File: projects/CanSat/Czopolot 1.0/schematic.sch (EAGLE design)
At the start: 6 parts

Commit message: File update
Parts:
- U$1: device PyBoard 1.1 footprint:PYBOARD1.1 -> SobieskiSat2:PYBOARD1.1
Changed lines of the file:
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@@
 </classes>
 <parts>
-<part name="U$1" library="PyBoard 1.1 footprint" deviceset="PYBOARD1.1" device=""/>
+<part name="U$1" library="SobieskiSat2" deviceset="PYBOARD1.1" device=""/>
 <part name="ULTIMATE_GPS" library="pinhead" library_urn="urn:adsk.eagle:library:325" deviceset="PINHD-1X4" device="" package3d_urn="urn:adsk.eagle:package:22407/2"/>
 <part name="U$2" library="SobieskiSat2" deviceset="SX1280" device="EXT" value="SX1280EXT"/>

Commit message: Work work..
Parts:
- U$2: value SX1280EXT -> SX1280; device SobieskiSat2:SX1280EXT -> SobieskiSat2:SX1280
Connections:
- new net BAT+: U$1.VBAT
- new net DIO1: U$1.X3, U$2.DIO1
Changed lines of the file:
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@@
 <part name="U$1" library="SobieskiSat2" deviceset="PYBOARD1.1" device=""/>
 <part name="ULTIMATE_GPS" library="pinhead" library_urn="urn:adsk.eagle:library:325" deviceset="PINHD-1X4" device="" package3d_urn="urn:adsk.eagle:package:22407/2"/>
-<part name="U$2" library="SobieskiSat2" deviceset="SX1280" device="EXT" value="SX1280EXT"/>
+<part name="U$2" library="SobieskiSat2" deviceset="SX1280" device="" value="SX1280"/>
 <part name="GND1" library="supply1" library_urn="urn:adsk.eagle:library:371" deviceset="GND" device=""/>
 <part name="X1" library="SobieskiSat2" deviceset="SMACONNECTOR" device="" package3d_urn="urn:adsk.eagle:package:6240946/1"/>
@@
 <part name="P+4" library="supply1" library_urn="urn:adsk.eagle:library:371" deviceset="VCC" device=""/>
 <part name="P+5" library="supply1" library_urn="urn:adsk.eagle:library:371" deviceset="VCC" device=""/>
+<part name="GND5" library="supply1" library_urn="urn:adsk.eagle:library:371" deviceset="GND" device=""/>
 </parts>
 <sheets>
@@
 <instance part="P+5" gate="VCC" x="-30.48" y="17.78" smashed="yes" rot="R90">
 <attribute name="VALUE" x="-27.94" y="15.24" size="1.778" layer="96" rot="R180"/>
+</instance>
+<instance part="GND5" gate="1" x="-50.8" y="7.62" smashed="yes" rot="R270">
+<attribute name="VALUE" x="-53.34" y="10.16" size="1.778" layer="96" rot="R270"/>
 </instance>
 </instances>
@@
 </segment>
 </net>
+<net name="BAT+" class="0">
+<segment>
+<pinref part="U$1" gate="G$1" pin="VBAT"/>
+<wire x1="-22.86" y1="7.62" x2="-25.4" y2="7.62" width="0.1524" layer="91"/>
+<label x="-25.4" y="7.62" size="1.778" layer="95" rot="R180" xref="yes"/>
+</segment>
+</net>
+<net name="BAT-" class="0">
+<segment>
+<pinref part="GND5" gate="1" pin="GND"/>
+<wire x1="-48.26" y1="7.62" x2="-45.72" y2="7.62" width="0.1524" layer="91"/>
+<label x="-45.72" y="7.62" size="1.778" layer="95" xref="yes"/>
+</segment>
+</net>
+<net name="DIO1" class="0">
+<segment>
+<pinref part="U$2" gate="G$1" pin="DIO1"/>
+<wire x1="5.08" y1="78.74" x2="5.08" y2="81.28" width="0.1524" layer="91"/>
+<label x="5.08" y="81.28" size="1.778" layer="95" rot="R90" xref="yes"/>
+</segment>
+<segment>
+<pinref part="U$1" gate="G$1" pin="X3"/>
+<wire x1="7.62" y1="30.48" x2="7.62" y2="33.02" width="0.1524" layer="91"/>
+<label x="7.62" y="33.02" size="1.778" layer="95" xref="yes"/>
+</segment>
+</net>

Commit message: Work work..
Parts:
- added JP1, JP2: (no value), pinhead:PINHD-1X2
- added Q1, Q2: (no value), adafruit:MOSFET-NGDS_TO220V
- added R1, R2: (no value), rcl:R-EU_0207/10
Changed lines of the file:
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@@
 <part name="P+5" library="supply1" library_urn="urn:adsk.eagle:library:371" deviceset="VCC" device=""/>
 <part name="GND5" library="supply1" library_urn="urn:adsk.eagle:library:371" deviceset="GND" device=""/>
+<part name="R1" library="rcl" library_urn="urn:adsk.eagle:library:334" deviceset="R-EU_" device="0207/10" package3d_urn="urn:adsk.eagle:package:23491/2"/>
+<part name="R2" library="rcl" library_urn="urn:adsk.eagle:library:334" deviceset="R-EU_" device="0207/10" package3d_urn="urn:adsk.eagle:package:23491/2"/>
+<part name="Q1" library="adafruit" library_urn="urn:adsk.eagle:library:420" deviceset="MOSFET-N" device="GDS_TO220V" package3d_urn="urn:adsk.eagle:package:6240882/1"/>
+<part name="Q2" library="adafruit" library_urn="urn:adsk.eagle:library:420" deviceset="MOSFET-N" device="GDS_TO220V" package3d_urn="urn:adsk.eagle:package:6240882/1"/>
+<part name="JP1" library="pinhead" library_urn="urn:adsk.eagle:library:325" deviceset="PINHD-1X2" device="" package3d_urn="urn:adsk.eagle:package:22435/2"/>
+<part name="JP2" library="pinhead" library_urn="urn:adsk.eagle:library:325" deviceset="PINHD-1X2" device="" package3d_urn="urn:adsk.eagle:package:22435/2"/>
 </parts>
 <sheets>
@@
 <instance part="GND5" gate="1" x="-50.8" y="7.62" smashed="yes" rot="R270">
 <attribute name="VALUE" x="-53.34" y="10.16" size="1.778" layer="96" rot="R270"/>
+</instance>
+<instance part="R1" gate="G$1" x="50.8" y="12.7" smashed="yes">
+<attribute name="NAME" x="46.99" y="14.1986" size="1.778" layer="95"/>
+<attribute name="VALUE" x="46.99" y="9.398" size="1.778" layer="96"/>
+</instance>
+<instance part="R2" gate="G$1" x="50.8" y="5.08" smashed="yes">
+<attribute name="NAME" x="46.99" y="6.5786" size="1.778" layer="95"/>
+<attribute name="VALUE" x="46.99" y="1.778" size="1.778" layer="96"/>
+</instance>
+<instance part="Q1" gate="G$1" x="66.04" y="12.7" smashed="yes">
+<attribute name="NAME" x="71.12" y="13.335" size="1.27" layer="95"/>
+<attribute name="VALUE" x="71.12" y="11.43" size="1.27" layer="96"/>
+</instance>
+<instance part="Q2" gate="G$1" x="66.04" y="0" smashed="yes">
+<attribute name="NAME" x="71.12" y="0.635" size="1.27" layer="95"/>
+<attribute name="VALUE" x="71.12" y="-1.27" size="1.27" layer="96"/>
+</instance>
+<instance part="JP1" gate="G$1" x="88.9" y="10.16" smashed="yes">
+<attribute name="NAME" x="82.55" y="15.875" size="1.778" layer="95"/>
+<attribute name="VALUE" x="82.55" y="5.08" size="1.778" layer="96"/>
+</instance>
+<instance part="JP2" gate="G$1" x="88.9" y="-5.08" smashed="yes">
+<attribute name="NAME" x="82.55" y="0.635" size="1.778" layer="95"/>
+<attribute name="VALUE" x="82.55" y="-10.16" size="1.778" layer="96"/>
 </instance>
 </instances>
@@
 packages will not be understood (or retained) with this version.
 </note>
+<note version="8.4" severity="warning">
+Since Version 8.4, EAGLE supports properties for SPICE simulation.
+Probes in schematics and SPICE mapping objects found in parts and library devices
+will not be understood with this version. Update EAGLE to the latest version
+for full support of SPICE simulation.
+</note>
 </compatibility>

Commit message: Work work..
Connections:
- new net V+: U$1.V+, ULTIMATE_GPS.1
- net VCC: no longer ULTIMATE_GPS.1
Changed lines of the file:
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@@
 <part name="P+2" library="supply1" library_urn="urn:adsk.eagle:library:371" deviceset="VCC" device=""/>
 <part name="P+3" library="supply1" library_urn="urn:adsk.eagle:library:371" deviceset="VCC" device=""/>
-<part name="P+4" library="supply1" library_urn="urn:adsk.eagle:library:371" deviceset="VCC" device=""/>
 <part name="P+5" library="supply1" library_urn="urn:adsk.eagle:library:371" deviceset="VCC" device=""/>
 <part name="GND5" library="supply1" library_urn="urn:adsk.eagle:library:371" deviceset="GND" device=""/>
@@
 <attribute name="VALUE" x="7.62" y="-58.42" size="1.778" layer="96" rot="R270"/>
 </instance>
-<instance part="P+4" gate="VCC" x="-5.08" y="-40.64" smashed="yes" rot="R270">
-<attribute name="VALUE" x="-7.62" y="-40.64" size="1.778" layer="96"/>
-</instance>
 <instance part="P+5" gate="VCC" x="-30.48" y="17.78" smashed="yes" rot="R90">
-<attribute name="VALUE" x="-27.94" y="15.24" size="1.778" layer="96" rot="R180"/>
+<attribute name="VALUE" x="-33.02" y="20.32" size="1.778" layer="96" rot="R270"/>
 </instance>
 <instance part="GND5" gate="1" x="-50.8" y="7.62" smashed="yes" rot="R270">
@@
 </segment>
 <segment>
-<pinref part="ULTIMATE_GPS" gate="A" pin="1"/>
-<wire x1="-7.62" y1="-50.8" x2="-7.62" y2="-40.64" width="0.1524" layer="91"/>
-<label x="-7.62" y="-45.72" size="1.778" layer="95" rot="R90"/>
-<pinref part="P+4" gate="VCC" pin="VCC"/>
-</segment>
-<segment>
 <pinref part="U$1" gate="G$1" pin="3V3"/>
 <pinref part="P+5" gate="VCC" pin="VCC"/>
@@
 </segment>
 </net>
+<net name="V+" class="0">
+<segment>
+<pinref part="U$1" gate="G$1" pin="V+"/>
+<wire x1="-22.86" y1="15.24" x2="-27.94" y2="15.24" width="0.1524" layer="91"/>
+<label x="-27.94" y="15.24" size="1.778" layer="95" rot="R180" xref="yes"/>
+</segment>
+<segment>
+<pinref part="ULTIMATE_GPS" gate="A" pin="1"/>
+<wire x1="-7.62" y1="-50.8" x2="-7.62" y2="-40.64" width="0.1524" layer="91"/>
+<label x="-7.62" y="-45.72" size="1.778" layer="95" rot="R90"/>
+</segment>
+</net>

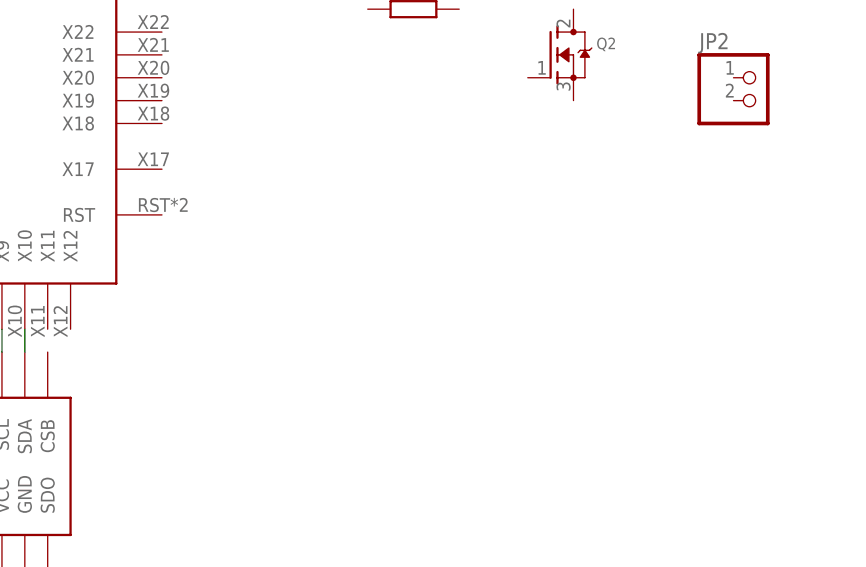
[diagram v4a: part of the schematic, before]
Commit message: Switch added
Duel switch and resistor added
Resistor type switched to another to match the grid
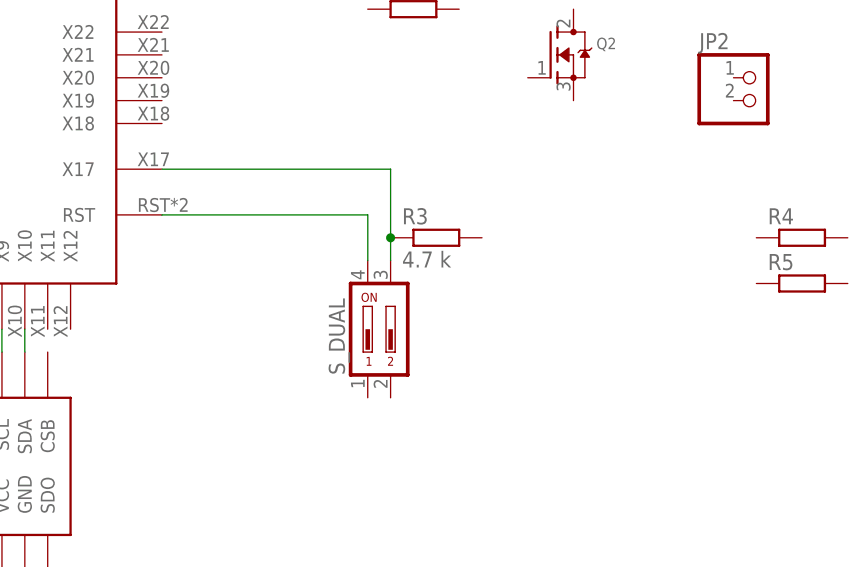
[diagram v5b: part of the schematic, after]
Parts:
- added R3: 4.7 k, rcl:R-EU_0204/7
- added R4: (no value), rcl:R-EU_0204/7
- added R5: (no value), rcl:R-EU_0207/10
- added U$5: SWITCH_DUAL, SobieskiSat2:SWITCH_DUAL
- R1, R2: device rcl:R-EU_0207/10 -> rcl:R-EU_0204/7
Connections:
- new net N$13: U$1.RST, U$5.4
- new net N$14: R3.1, U$1.X17, U$5.3
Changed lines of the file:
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@@
 <?xml version="1.0" encoding="utf-8"?>
 <!DOCTYPE eagle SYSTEM "eagle.dtd">
-<eagle version="9.5.1">
+<eagle version="9.5.2">
 <drawing>
 <settings>
@@
 <part name="P+5" library="supply1" library_urn="urn:adsk.eagle:library:371" deviceset="VCC" device=""/>
 <part name="GND5" library="supply1" library_urn="urn:adsk.eagle:library:371" deviceset="GND" device=""/>
-<part name="R1" library="rcl" library_urn="urn:adsk.eagle:library:334" deviceset="R-EU_" device="0207/10" package3d_urn="urn:adsk.eagle:package:23491/2"/>
-<part name="R2" library="rcl" library_urn="urn:adsk.eagle:library:334" deviceset="R-EU_" device="0207/10" package3d_urn="urn:adsk.eagle:package:23491/2"/>
+<part name="R1" library="rcl" library_urn="urn:adsk.eagle:library:334" deviceset="R-EU_" device="0204/7" package3d_urn="urn:adsk.eagle:package:23498/2"/>
+<part name="R2" library="rcl" library_urn="urn:adsk.eagle:library:334" deviceset="R-EU_" device="0204/7" package3d_urn="urn:adsk.eagle:package:23498/2"/>
 <part name="Q1" library="adafruit" library_urn="urn:adsk.eagle:library:420" deviceset="MOSFET-N" device="GDS_TO220V" package3d_urn="urn:adsk.eagle:package:6240882/1"/>
 <part name="Q2" library="adafruit" library_urn="urn:adsk.eagle:library:420" deviceset="MOSFET-N" device="GDS_TO220V" package3d_urn="urn:adsk.eagle:package:6240882/1"/>
 <part name="JP1" library="pinhead" library_urn="urn:adsk.eagle:library:325" deviceset="PINHD-1X2" device="" package3d_urn="urn:adsk.eagle:package:22435/2"/>
 <part name="JP2" library="pinhead" library_urn="urn:adsk.eagle:library:325" deviceset="PINHD-1X2" device="" package3d_urn="urn:adsk.eagle:package:22435/2"/>
+<part name="U$5" library="SobieskiSat2" deviceset="SWITCH_DUAL" device=""/>
+<part name="R3" library="rcl" library_urn="urn:adsk.eagle:library:334" deviceset="R-EU_" device="0204/7" package3d_urn="urn:adsk.eagle:package:23498/2" value="4.7 k"/>
+<part name="R4" library="rcl" library_urn="urn:adsk.eagle:library:334" deviceset="R-EU_" device="0204/7" package3d_urn="urn:adsk.eagle:package:23498/2"/>
+<part name="R5" library="rcl" library_urn="urn:adsk.eagle:library:334" deviceset="R-EU_" device="0207/10" package3d_urn="urn:adsk.eagle:package:23491/2"/>
 </parts>
 <sheets>
@@
 <attribute name="NAME" x="82.55" y="0.635" size="1.778" layer="95"/>
 <attribute name="VALUE" x="82.55" y="-10.16" size="1.778" layer="96"/>
+</instance>
+<instance part="U$5" gate="G$1" x="45.72" y="-30.48" smashed="yes"/>
+<instance part="R3" gate="G$1" x="53.34" y="-20.32" smashed="yes">
+<attribute name="NAME" x="49.53" y="-18.8214" size="1.778" layer="95"/>
+<attribute name="VALUE" x="49.53" y="-23.622" size="1.778" layer="96"/>
+</instance>
+<instance part="R4" gate="G$1" x="93.98" y="-20.32" smashed="yes">
+<attribute name="NAME" x="90.17" y="-18.8214" size="1.778" layer="95"/>
+<attribute name="VALUE" x="90.17" y="-23.622" size="1.778" layer="96"/>
+</instance>
+<instance part="R5" gate="G$1" x="93.98" y="-25.4" smashed="yes">
+<attribute name="NAME" x="90.17" y="-23.9014" size="1.778" layer="95"/>
+<attribute name="VALUE" x="90.17" y="-28.702" size="1.778" layer="96"/>
 </instance>
 </instances>
@@
 </segment>
 </net>
+<net name="N$13" class="0">
+<segment>
+<pinref part="U$5" gate="G$1" pin="4"/>
+<pinref part="U$1" gate="G$1" pin="RST"/>
+<wire x1="45.72" y1="-22.86" x2="45.72" y2="-17.78" width="0.1524" layer="91"/>
+<wire x1="45.72" y1="-17.78" x2="22.86" y2="-17.78" width="0.1524" layer="91"/>
+</segment>
+</net>
+<net name="N$14" class="0">
+<segment>
+<pinref part="U$5" gate="G$1" pin="3"/>
+<pinref part="U$1" gate="G$1" pin="X17"/>
+<wire x1="48.26" y1="-22.86" x2="48.26" y2="-20.32" width="0.1524" layer="91"/>
+<wire x1="48.26" y1="-20.32" x2="48.26" y2="-12.7" width="0.1524" layer="91"/>
+<wire x1="48.26" y1="-12.7" x2="22.86" y2="-12.7" width="0.1524" layer="91"/>
+<pinref part="R3" gate="G$1" pin="1"/>
+<junction x="48.26" y="-20.32"/>
+</segment>
+</net>

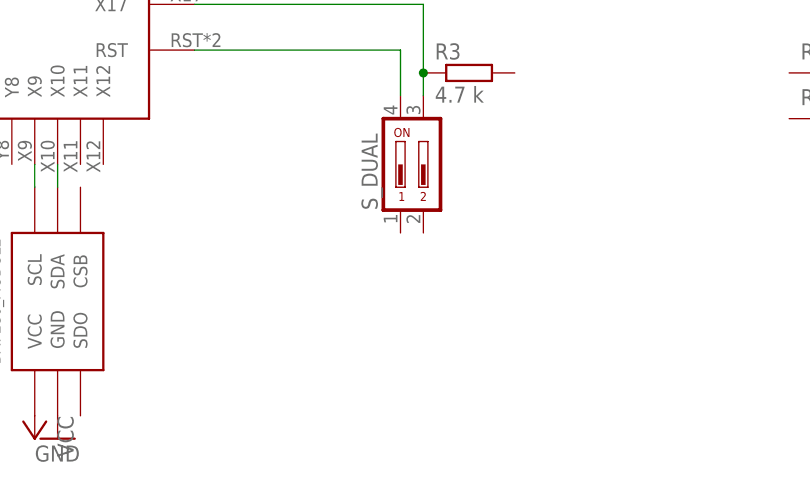
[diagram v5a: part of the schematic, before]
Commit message: Added GND to switch
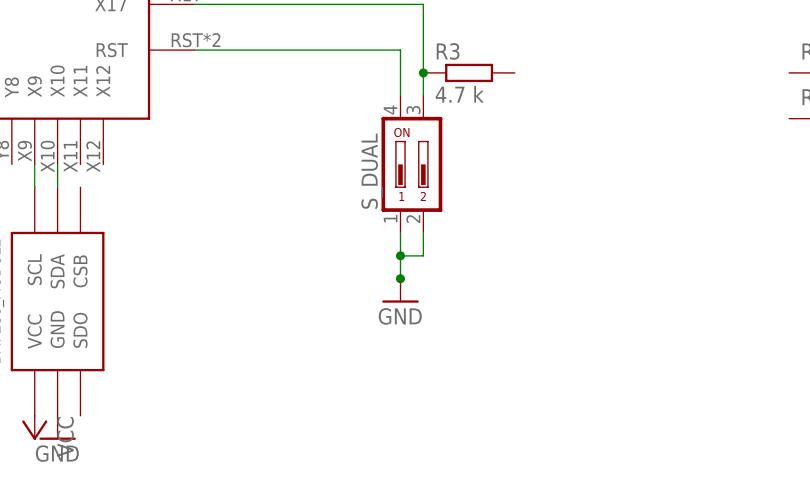
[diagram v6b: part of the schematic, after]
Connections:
- net GND: now also U$5.1, U$5.2
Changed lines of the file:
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@@
 <part name="R4" library="rcl" library_urn="urn:adsk.eagle:library:334" deviceset="R-EU_" device="0204/7" package3d_urn="urn:adsk.eagle:package:23498/2"/>
 <part name="R5" library="rcl" library_urn="urn:adsk.eagle:library:334" deviceset="R-EU_" device="0207/10" package3d_urn="urn:adsk.eagle:package:23491/2"/>
+<part name="GND6" library="supply1" library_urn="urn:adsk.eagle:library:371" deviceset="GND" device=""/>
 </parts>
 <sheets>
@@
 <attribute name="VALUE" x="90.17" y="-28.702" size="1.778" layer="96"/>
 </instance>
+<instance part="GND6" gate="1" x="45.72" y="-45.72" smashed="yes">
+<attribute name="VALUE" x="43.18" y="-48.26" size="1.778" layer="96"/>
+</instance>
 </instances>
 <busses>
@@
 <pinref part="GND4" gate="1" pin="GND"/>
 </segment>
+<segment>
+<pinref part="GND6" gate="1" pin="GND"/>
+<junction x="45.72" y="-43.18"/>
+<pinref part="U$5" gate="G$1" pin="1"/>
+<wire x1="45.72" y1="-38.1" x2="45.72" y2="-40.64" width="0.1524" layer="91"/>
+<pinref part="U$5" gate="G$1" pin="2"/>
+<wire x1="45.72" y1="-40.64" x2="45.72" y2="-43.18" width="0.1524" layer="91"/>
+<wire x1="48.26" y1="-38.1" x2="48.26" y2="-40.64" width="0.1524" layer="91"/>
+<wire x1="48.26" y1="-40.64" x2="45.72" y2="-40.64" width="0.1524" layer="91"/>
+<junction x="45.72" y="-40.64"/>
+</segment>
 </net>
